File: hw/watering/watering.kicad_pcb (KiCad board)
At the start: 2 copper layers, 96.8 x 50.1 mm, 110 parts, among them J2 USB_C_Receptacle, J3 Conn_01x02_Pin, J4 Conn_01x02_Pin, J6 Conn_01x02_Pin, Q1 2N7002, SW2 KMS221GLFS, SW3 KMS221GLFS, U1 ESP32-C6, U10 MCP6002-xSN, U11 STI3508, U3 W25Q128JVS, U4 STI3508, U5 STI3508, U6 STI3508, U7 NCP163AFCT330T2G, U8 MCP6002-xSN, U9 MCP6002-xSN, Y1 40MHz, Y2 32768Hz

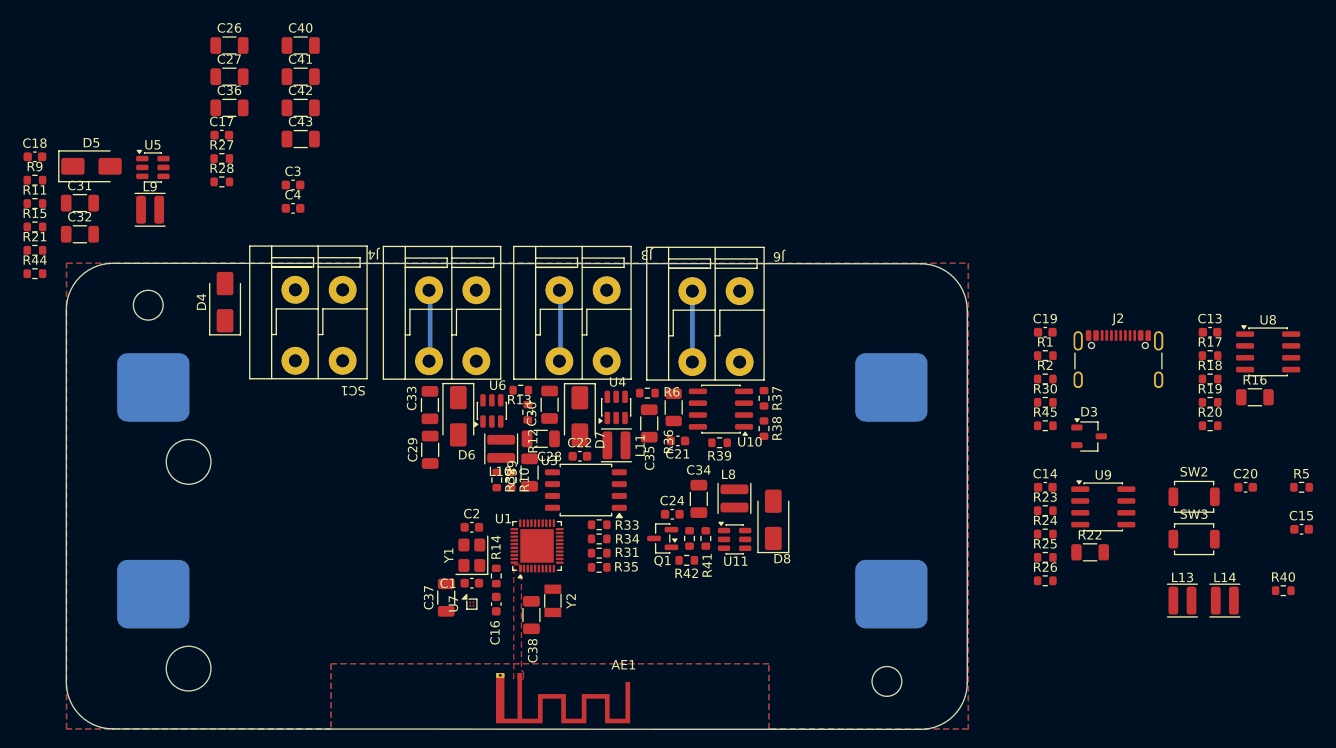
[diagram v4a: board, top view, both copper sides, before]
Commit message: reduced pcb size
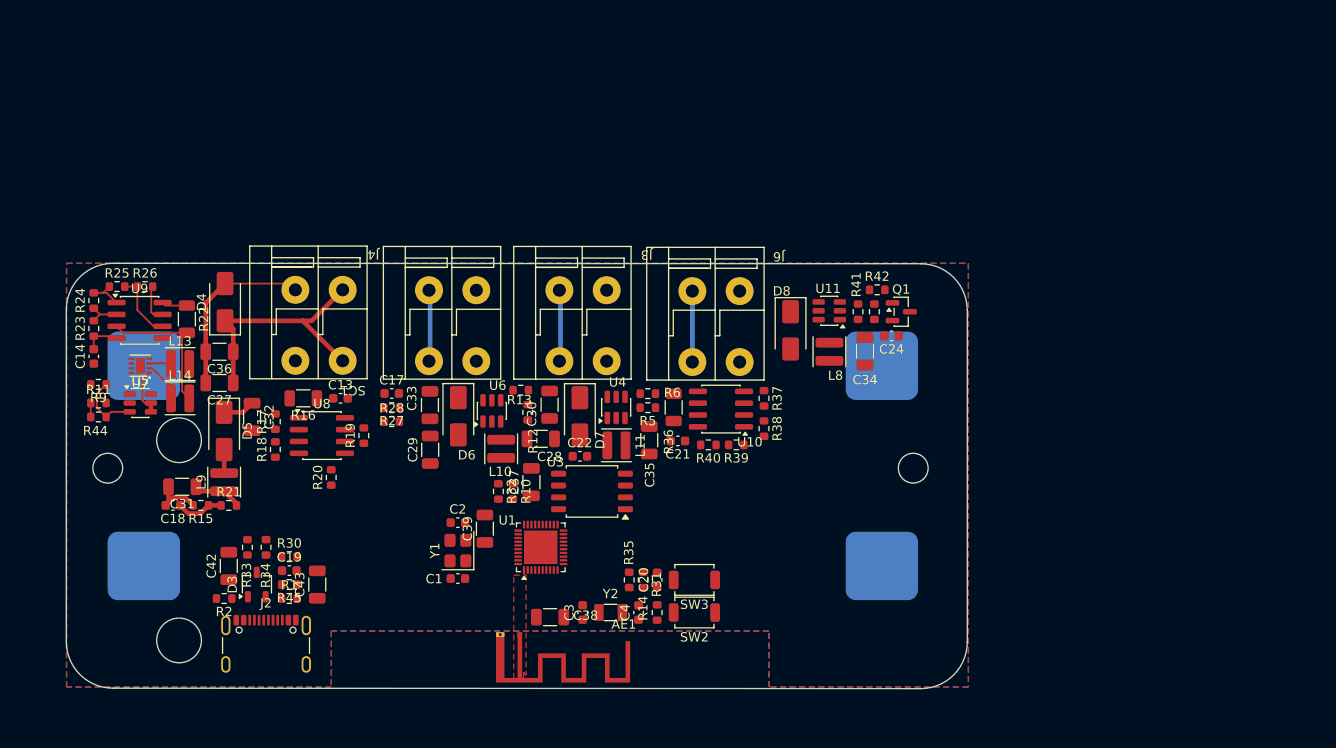
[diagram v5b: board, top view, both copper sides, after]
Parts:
- removed C15, C16: 1u, Capacitor_SMD:C_0603_1608Metric
- removed C26, C40, C41: 22u, Capacitor_SMD:C_1206_3216Metric
- U7: value NCP163AFCT330T2G -> DRV8220DSG; footprint Package_CSP:WLCSP-4_0.64x0.64mm_Layout2x2_P0.35mm -> Package_SON:Texas_DSG0008A_WSON-8-1EP_2x2mm_P0.5mm_EP0.9x1.6mm
- moved L14 114.3 mm to (149.8, 114.5)
- moved L13 110.6 mm to (149.8, 110.8)
- moved U9 105.4 mm to (145.4, 106.1)
- moved R24 105.2 mm to (140.5, 104.0), turned to 90 degrees
- moved R23 104.0 mm to (140.5, 107.0), turned to 90 degrees
- moved R25 103.8 mm to (143.0, 102.5)
- moved C14 103.1 mm to (140.5, 110.0), turned to 90 degrees
- moved R16 102.2 mm to (163.0, 114.5), turned to 180 degrees
- moved U8 102.0 mm to (165.0, 118.5)
- moved R26 101.7 mm to (146.0, 102.5)
- moved R18 100.7 mm to (160.0, 120.0), turned to 90 degrees
- moved R17 100.6 mm to (160.0, 117.0), turned to 90 degrees
- moved R22 100.2 mm to (150.5, 106.0), turned to -90 degrees
- moved J2 96.5 mm to (159.0, 142.0)
- moved R20 94.5 mm to (166.0, 123.0), turned to 90 degrees
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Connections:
- C28 pad 1: /+3V3 -> /V_bat
- C29 pad 1: /+3V3 -> /V_bat
- L10 pad 1: /+3V3 -> /V_bat
- L11 pad 1: /+3V3 -> /V_bat
- L13 pad 1: Net-(U2-OUT2) -> Net-(U7-OUT2)
- L14 pad 1: Net-(U2-OUT1) -> Net-(U7-OUT1)
- U4 pad 5: /+3V3 -> /V_bat
- U6 pad 5: /+3V3 -> /V_bat
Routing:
- net /GND: track 0.00 -> 29.1 mm
- net /solar/+Vsolar: track 0.00 -> 27.1 mm
- net /solar/current_meas1/i_out: track 0.00 -> 15.8 mm
- net /V_bat: track 0.00 -> 10.6 mm
- net Net-(U9B--): track 0.00 -> 7.31 mm
- net /solar/bat/0V6: track 0.00 -> 7.09 mm
- net /controller/V_bat_meas: track 0.00 -> 5.12 mm
- net Net-(U7-OUT1): track 0.00 -> 4.40 mm
- net /controller/i_usb_meas: track 0.00 -> 4.13 mm
- net Net-(R24-Pad2): track 0.00 -> 3.83 mm
- net Net-(U9A--): track 0.00 -> 3.68 mm
- net /+3V3: track 0.00 -> 3.40 mm
- net /+5V: track 0.00 -> 2.74 mm
- net Net-(D5-A): track 0.00 -> 2.53 mm
- net Net-(U7-OUT2): track 0.00 -> 2.38 mm
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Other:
- board size 96.8 x 50.1 mm -> 96.8 x 45.7 mm

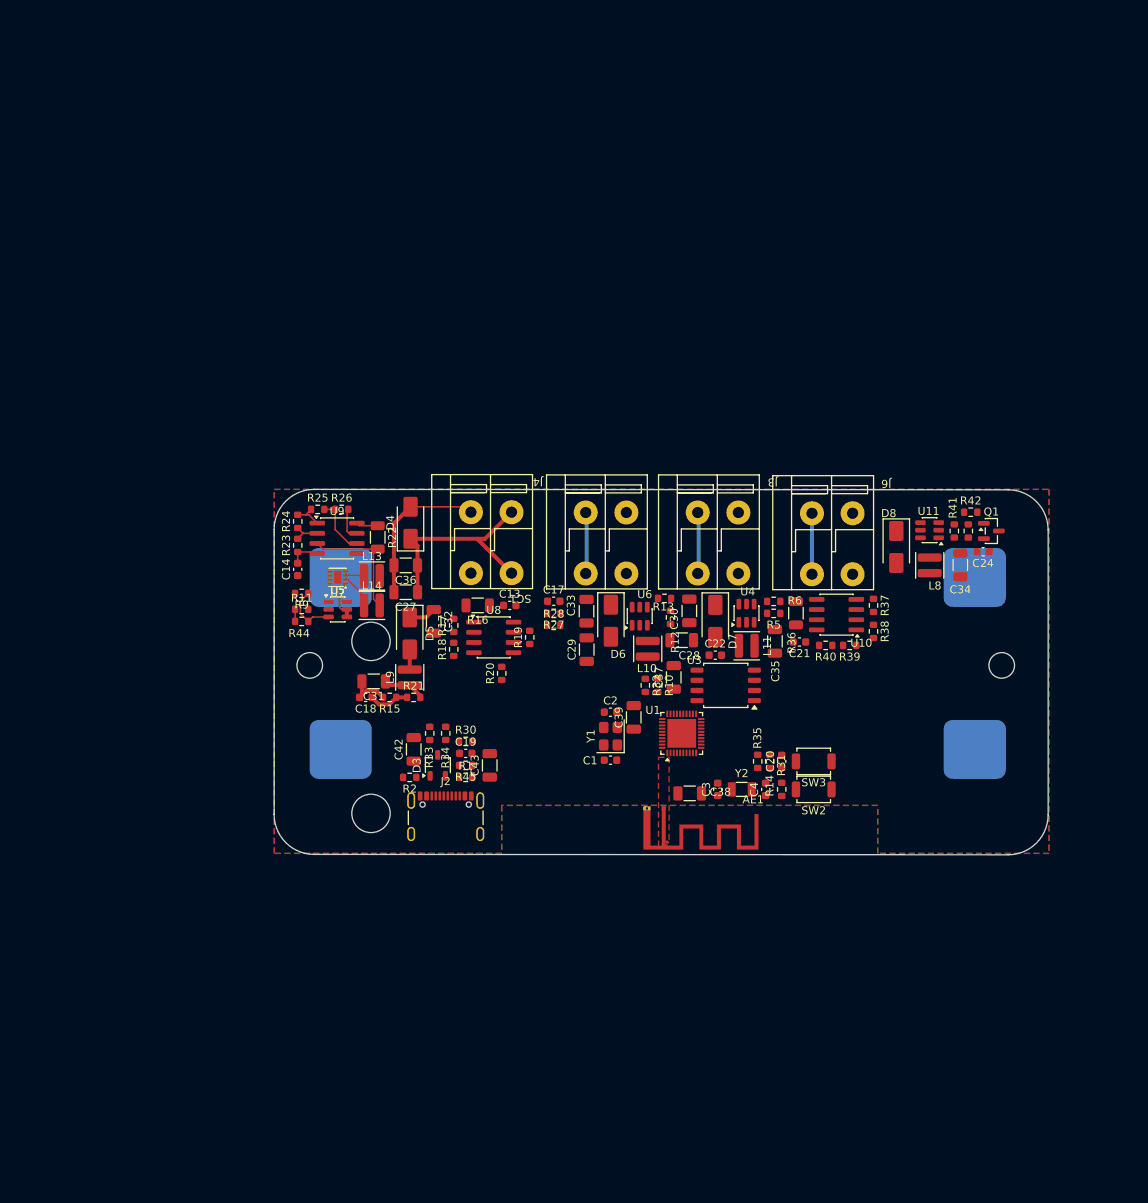
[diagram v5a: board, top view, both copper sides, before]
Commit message: - hw   - rewired power input for battery   - some first placing of parts on pcb but no routing - sw   - added example http server from examples to server.cpp, not compilable yet
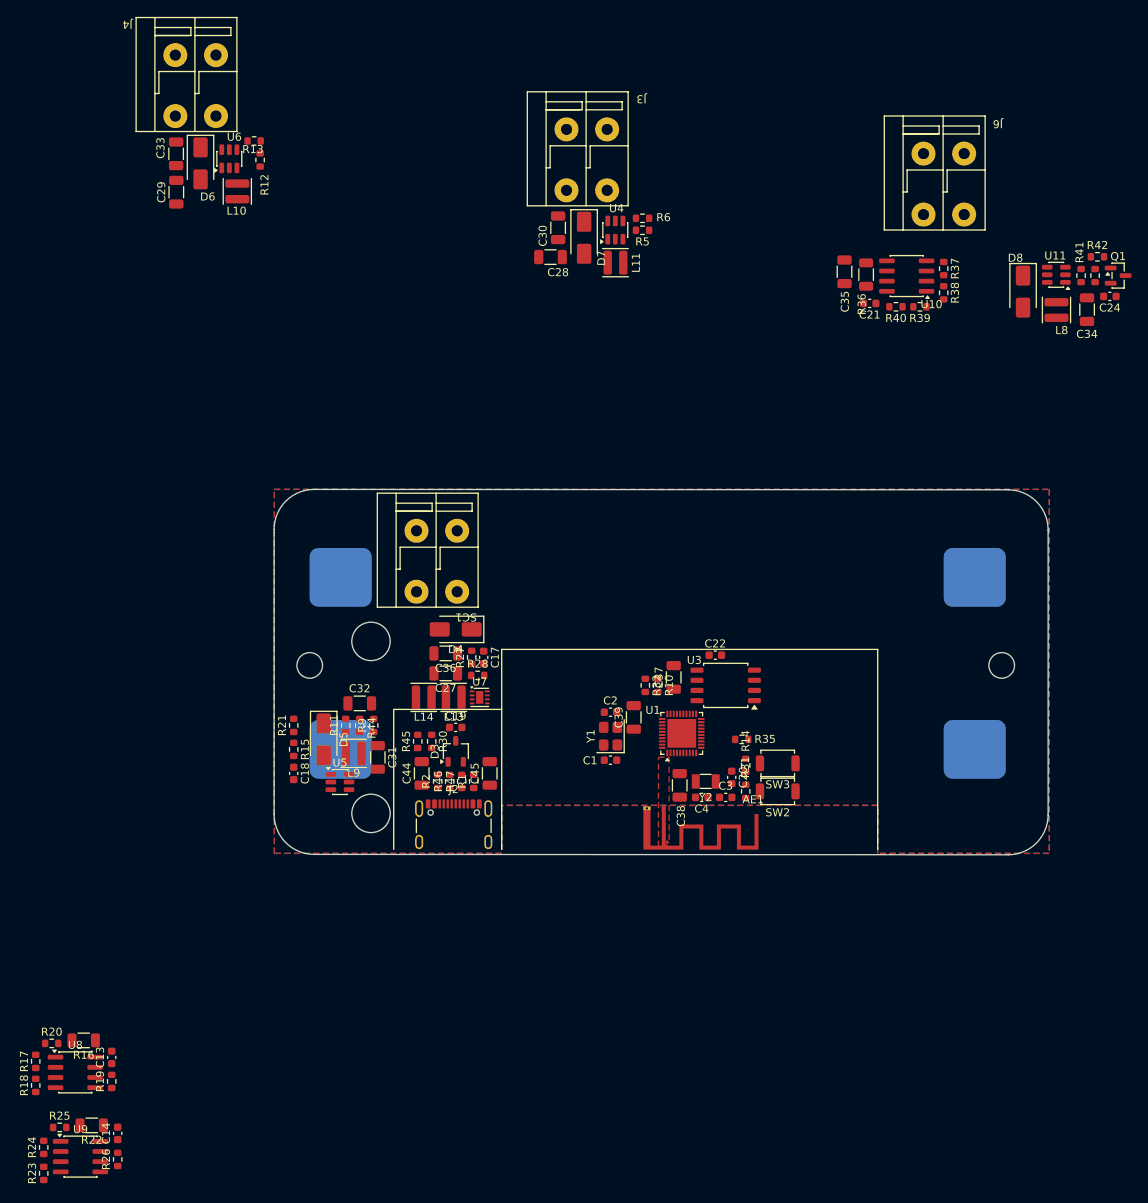
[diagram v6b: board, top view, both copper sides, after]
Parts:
- removed C42, C43: 22u, Capacitor_SMD:C_1206_3216Metric
- removed R33, R34: 47, Resistor_SMD:R_0603_1608Metric
- added C44: 22u, Capacitor_SMD:C_1206_3216Metric, F.Cu at (156.0, 135.5)
- added C45: 22u, Capacitor_SMD:C_1206_3216Metric, F.Cu at (164.5, 135.5)
- added R46: 47, Resistor_SMD:R_0603_1608Metric, F.Cu at (159.5, 136.5)
- added R47: 47, Resistor_SMD:R_0603_1608Metric, F.Cu at (161.0, 136.5)
- moved R26 85.9 mm to (118.0, 183.8), turned to 90 degrees
- moved R23 84.7 mm to (108.8, 185.5)
- moved R24 84.4 mm to (108.8, 182.2)
- moved R25 83.7 mm to (110.8, 179.8)
- moved U9 83.7 mm to (113.3, 183.4)
- moved R22 81.7 mm to (114.8, 179.5), turned to 180 degrees
- moved C29 76.8 mm to (125.3, 62.9)
- moved C33 76.8 mm to (125.3, 58.0)
- moved D6 76.8 mm to (128.3, 59.2)
- moved J4 76.8 mm to (127.9, 49.5)
- moved L10 76.8 mm to (132.9, 62.8)
- moved R12 76.8 mm to (135.8, 58.8)
- moved R13 76.8 mm to (135.1, 56.5)
- moved U6 76.8 mm to (131.9, 58.7)
- moved R19 76.2 mm to (117.2, 174.0)
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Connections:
- net /V_usb_avail renamed /controller/V_usb_avail
- J2 pad A6: /controller/USBDP -> Net-(J2-D+-PadA6)
- J2 pad A7: /controller/USBDM -> Net-(J2-D--PadA7)
- J2 pad B6: /controller/USBDP -> Net-(J2-D+-PadA6)
- J2 pad B7: /controller/USBDM -> Net-(J2-D--PadA7)
- U1 pad 13: unconnected-(U1-MTDO/GPIO7/FSPID-Pad13) -> /controller/power-enable
- U1 pad 18: Net-(U1-GPIO12/USB_D-) -> /controller/USBDM
- U1 pad 19: Net-(U1-GPIO13/USB_D+) -> /controller/USBDP
- U5 pad 4: /V_bat -> /solar/power_enable
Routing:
- net /GND: track 29.1 -> 0.00 mm
- net /solar/+Vsolar: track 27.1 -> 0.00 mm
- net /solar/current_meas1/i_out: track 15.8 -> 0.00 mm
- net /V_bat: track 10.6 -> 0.00 mm
- net /valves2/24V: track 7.62 -> 0.00 mm
- net /valves1/24V: track 7.62 -> 0.00 mm
- net /conductivity/current_meas/i_out: track 7.62 -> 0.00 mm
- net Net-(U9B--): track 7.31 -> 0.00 mm
- net /solar/bat/0V6: track 7.09 -> 0.00 mm
- net /controller/V_bat_meas: track 5.12 -> 0.00 mm
- net Net-(U7-OUT1): track 4.40 -> 0.00 mm
- net /controller/i_usb_meas: track 4.13 -> 0.00 mm
- net Net-(R24-Pad2): track 3.83 -> 0.00 mm
- net Net-(U9A--): track 3.68 -> 0.00 mm
- net /+3V3: track 3.40 -> 0.00 mm
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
